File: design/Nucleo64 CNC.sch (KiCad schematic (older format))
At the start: 98 parts, among them J1 YMotor, J10 ZB, J11 AA, J12 AB, J13 VMOT, J14 Spindle/Coolant, J15 Control, J16 I2C, J17 UART/GPIO, J18 Limits, J19 GPIO, J2 XMotor, J20 Power out, J21 SDCARD/GPIO, J23 Reset, J24 DC Spindle, J3 ZMotor, J4 AMotor, J5 YA, J6 YB, J7 XA, J8 XB, J9 ZA, Q1 2N7002, Q2 IRLML6402, Q3 2N7002, U1 NUCLEO64-F411RE, U10 74LVC2G17, U2 TLP290-4, U3 TLP290-4, U4 TLP290-4, U5 24LC16, U6 TCA9406, U7 ULN2003, U8 TLP290-4, U9 74LVC1G17

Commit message: Updated
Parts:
- added C8: 2u2, Capacitor_SMD:C_1206_3216Metric, symbol Device:C
- added C9: 1u, Capacitor_SMD:C_1206_3216Metric, symbol Device:C
- added R37: 1M, Resistor_SMD:R_0805_2012Metric, symbol Device:R
- added U11: 74LVC1G17, Package_TO_SOT_SMD:SOT-353_SC-70-5, symbol IoEngineering:74LVC1G17
- added U12: TPS709, Package_TO_SOT_SMD:SOT-23-5, symbol Regulator_Linear:TC1017-xCT
- Lk6: value DC Spindle -> LDObypass
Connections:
- net +3V3: now also U9.5 (VCC)
- net +5V: now also U11.5 (VCC); no longer R1.1, R2.1, R24.1, R4.1, R5.1, R6.1, R7.1, R8.1, R9.1
- net AuxIn0: now also U1.66 (PB14); no longer U1.64 (PB15)
- net AuxIn1: now also U1.17 (PA15); no longer U1.60 (PB2)
- net AuxOut0: now also U1.64 (PB15); no longer U1.66 (PB14)
- net AuxOut1: now also U1.60 (PB2); no longer U1.63 (PB10)
- net Flood: now also U1.63 (PB10); no longer U1.65 (PB4)
- net GND: now also U9.3 (GND), R37.2, U11.3 (GND); no longer J15.1 (Pin_1), J15.3 (Pin_3), J15.5 (Pin_5), J15.7 (Pin_7), J15.9 (Pin_9), J18.1 (Pin_1), J18.3 (Pin_3), J18.5 (Pin_5), J18.7 (Pin_7), U2.11, U2.13, U2.15, U2.9, U3.11, U3.13, U3.15, U3.9, U8.9
- net Mist: now also U1.65 (PB4); no longer U1.68 (PB13)
- net STDiag1: now also U1.68 (PB13); no longer U1.17 (PA15)
- net SpindlePWM: now also U11.2; no longer J14.16 (Pin_16), Lk6.1 (Pin_1)
- net at U4.10, U4.12, U4.14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: now also Lk6.2 (Pin_2), C8.1, U12.5 (VOUT); no longer Lk1.2 (Pin_2), U7.9 (COM)
- net GNDS: now reaches J14.1 (Pin_1), J14.11 (Pin_11), J14.13 (Pin_13), J14.3 (Pin_3), J14.5 (Pin_5), J14.7 (Pin_7), J14.9 (Pin_9), Lk3.2 (Pin_2), U7.7 (I7), U7.8 (GND)
- net GNDS: now also J15.1 (Pin_1), J15.3 (Pin_3), J15.5 (Pin_5), J15.7 (Pin_7), J15.9 (Pin_9), J18.1 (Pin_1), J18.3 (Pin_3), J18.5 (Pin_5), J18.7 (Pin_7), U2.11, U2.13, U2.15, U2.9, U3.11, U3.13, U3.15, U3.9, U8.9, C8.2, C9.2, R37.1, U12.2 (GND)
- net SpindlePWMOut: now reaches U8.6
- net SpindlePWMOut: now also J14.16 (Pin_16), U11.4; no longer Lk6.2 (Pin_2)
- new net Vdrive: C9.1, Lk1.2 (Pin_2), Lk6.1 (Pin_1), R1.1, R2.1, R24.1, R4.1, R5.1, R6.1, R7.1, R8.1, R9.1, U12.1 (VIN)
- no-connect marks 10 -> 11
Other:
- moved on the sheet: Lk1, Lk7, U9

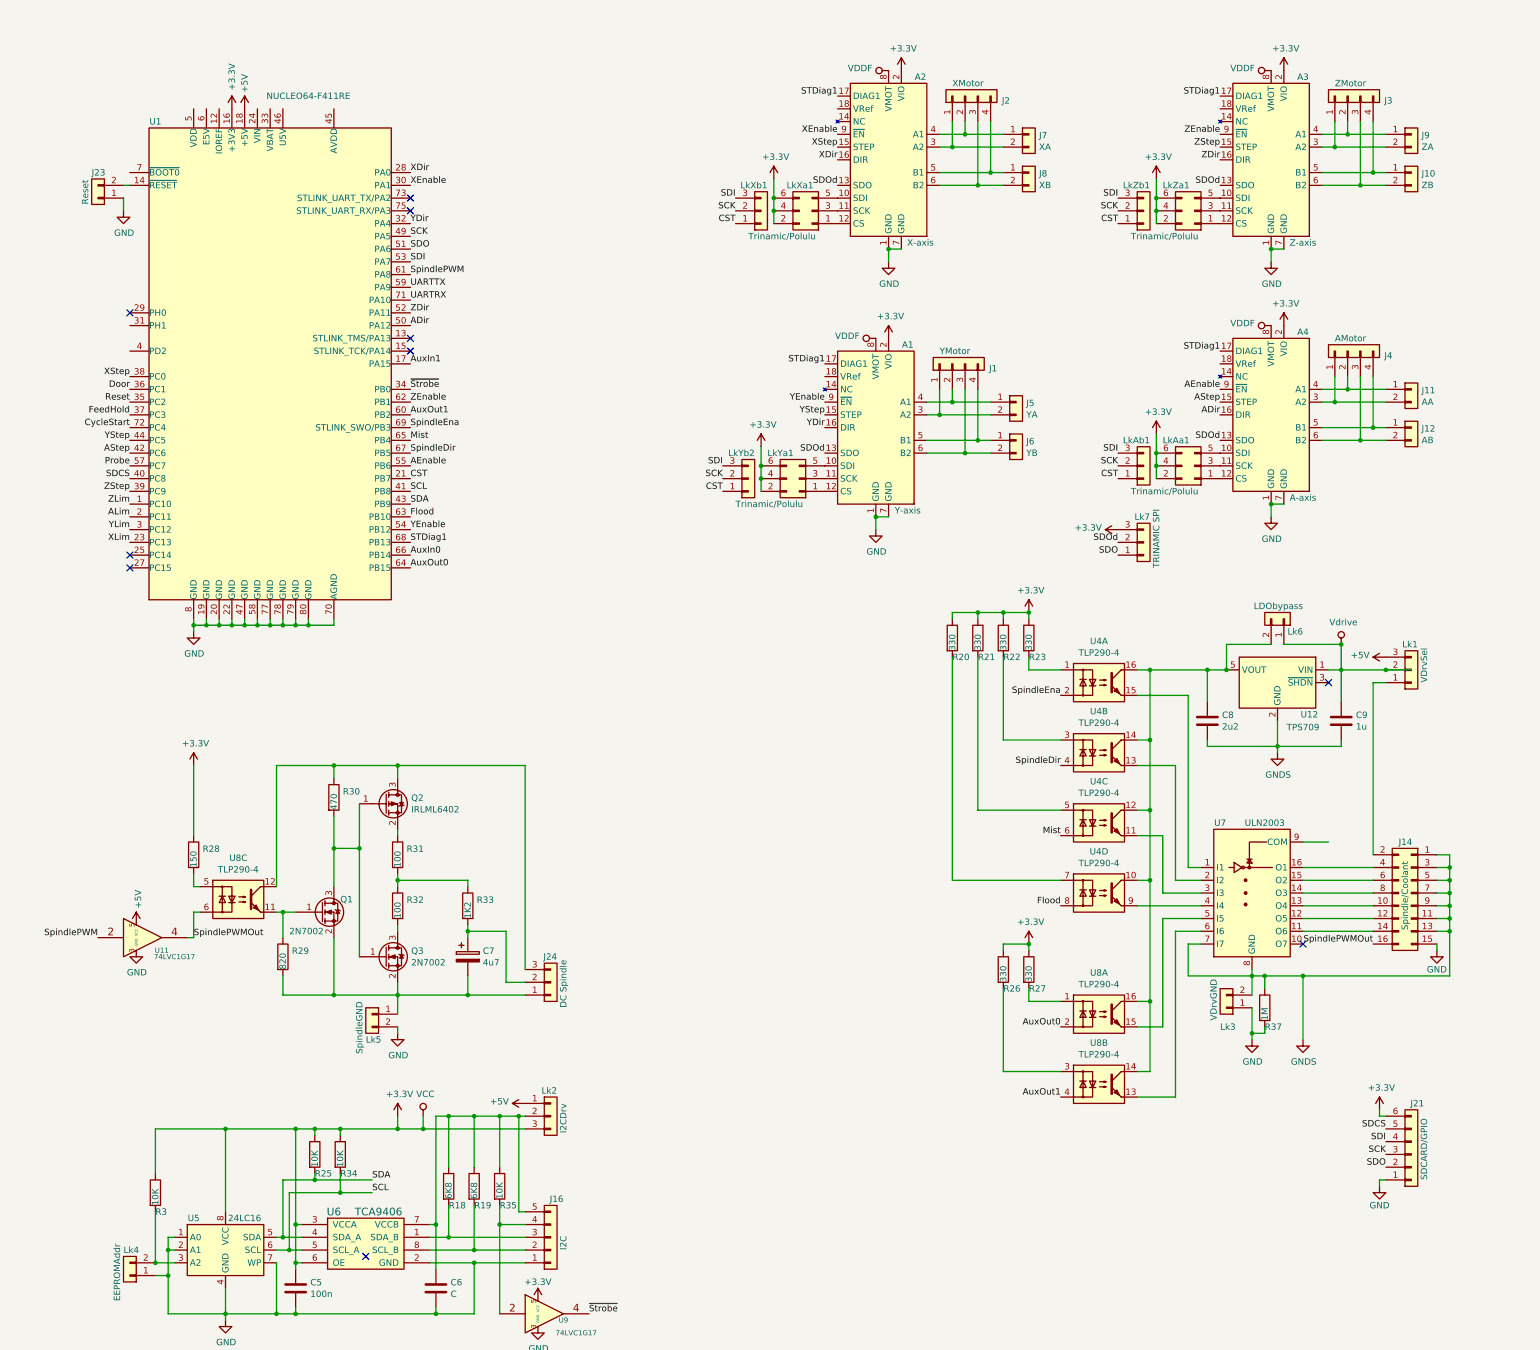
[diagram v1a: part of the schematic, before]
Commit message: Updated to version sent for small prototype batch
Design and board map file to be verified with this batch.
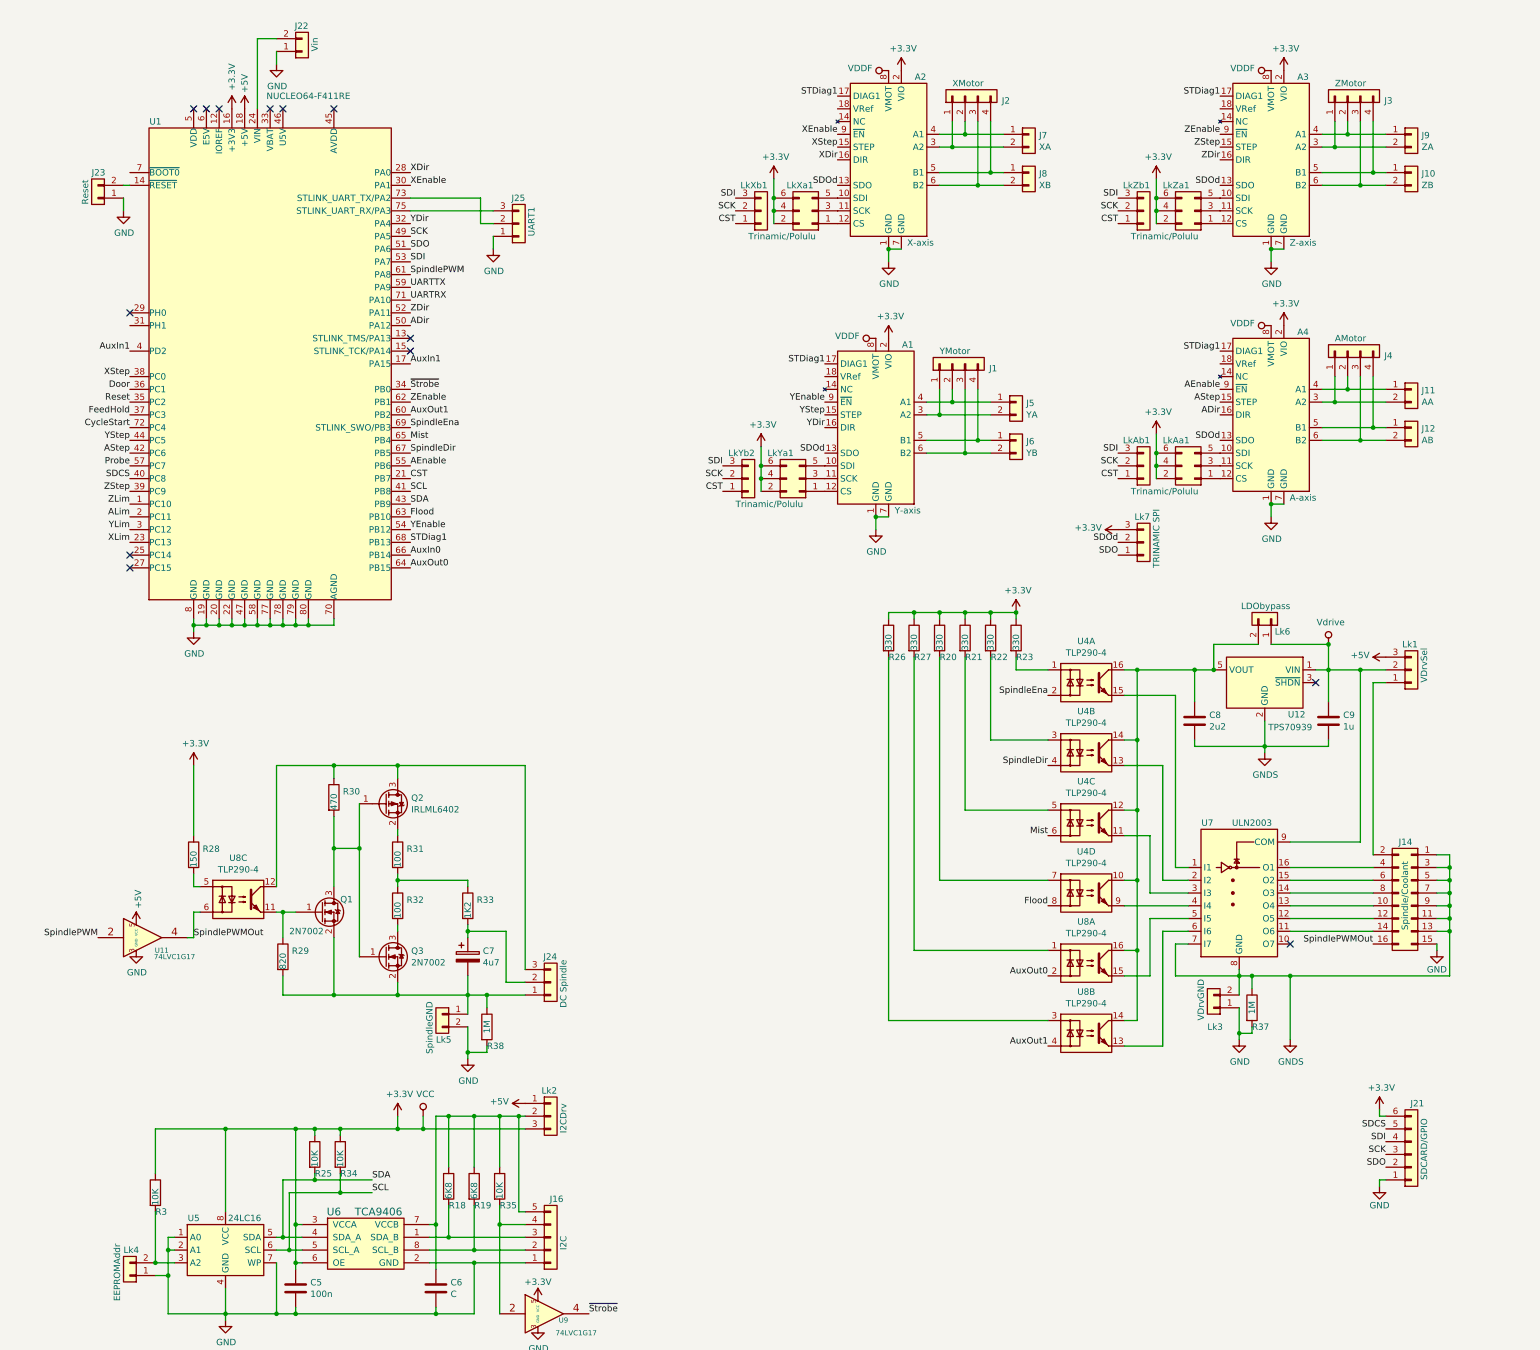
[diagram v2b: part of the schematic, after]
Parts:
- added J22: Vin, Connector_PinHeader_2.54mm:PinHeader_1x02_P2.54mm_Vertical, symbol Connector_Generic:Conn_01x02
- added J25: UART1, Connector_PinHeader_2.54mm:PinHeader_1x03_P2.54mm_Vertical, symbol Connector_Generic:Conn_01x03
- added R38: 1M, Resistor_SMD:R_0805_2012Metric, symbol Device:R
- U12: value TPS709 -> TPS70939
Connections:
- net AuxIn1: now also U1.4 (PD2)
- net GND: now also J22.1 (Pin_1), J25.1 (Pin_1), R38.2
- net Vdrive: now also U7.9 (COM)
- net at U1.24 (VIN): now also J22.2 (Pin_2)
- net at U1.73 (STLINK_UART_TX/PA2): now also J25.2 (Pin_2)
- net at U1.75 (STLINK_UART_RX/PA3): now also J25.3 (Pin_3)
- net at C7.2, J24.1 (Pin_1), Lk5.1 (Pin_1)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: now also R38.1
- no-connect marks 11 -> 14
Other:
- moved on the sheet: C8, C9, Lk3, Lk5, Lk6, R20, R21, R22, R23, R26, R27, R37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

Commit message: Updated to v1.0c
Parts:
- added Lk10, Lk11, Lk12, Lk9: AA, Connector_PinHeader_2.54mm:PinHeader_1x02_P2.54mm_Vertical, symbol Connector_Generic:Conn_01x02
- added Lk13: TMC UART, Connector_PinHeader_2.54mm:PinHeader_1x02_P2.54mm_Vertical, symbol Connector_Generic:Conn_01x02
- added Lk8: TMC UART/SPI, Connector_PinHeader_2.54mm:PinHeader_1x03_P2.54mm_Vertical, symbol Connector_Generic:Conn_01x03
- added R39: 1K, Resistor_SMD:R_0805_2012Metric, symbol Device:R
- added R40: 470, Resistor_SMD:R_0805_2012Metric, symbol Device:R
- added R41: 2K2, Resistor_SMD:R_0805_2012Metric, symbol Device:R
- added R42, R43: 10K, Resistor_SMD:R_0805_2012Metric, symbol Device:R
- added U13: VOM452, Package_SO:MFSOP6-5_4.4x3.6mm_P1.27mm, symbol IoEngineering:VOM452
- C7: value 4u7 -> 10u
- J17: value UART/GPIO -> UART
- J19: footprint Connector_PinHeader_2.54mm:PinHeader_1x03_P2.54mm_Vertical -> Connector_PinHeader_2.54mm:PinHeader_1x04_P2.54mm_Vertical; symbol Connector_Generic:Conn_01x03 -> Connector_Generic:Conn_01x04
- Lk7: value TRINAMIC SPI -> TMC DATA
- R28: value 150 -> 470
- R30: value 470 -> 1K2
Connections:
- net +3V3: now also LkAa1.1 (Pin_1), LkAa1.3 (Pin_3), LkAa1.5 (Pin_5), LkXa1.1 (Pin_1), LkXa1.3 (Pin_3), LkXa1.5 (Pin_5), LkYa1.1 (Pin_1), LkYa1.3 (Pin_3), LkYa1.5 (Pin_5), LkZa1.1 (Pin_1), LkZa1.3 (Pin_3), LkZa1.5 (Pin_5), R41.1; no longer LkAa1.2 (Pin_2), LkAa1.4 (Pin_4), LkAa1.6 (Pin_6), LkXa1.2 (Pin_2), LkXa1.4 (Pin_4), LkXa1.6 (Pin_6), LkYa1.2 (Pin_2), LkYa1.4 (Pin_4), LkYa1.6 (Pin_6), LkZa1.2 (Pin_2), LkZa1.4 (Pin_4), LkZa1.6 (Pin_6), R28.1
- net +5V: now also R28.1
- net ALim: now also A4.17 (DIAG1)
- net GND: now also R42.2, R43.2
- net GNDS: now also U8.11
- net Probe: now also U8.12; no longer U8.10
- net SDI: no longer LkAb1.3 (Pin_3), LkYb2.3 (Pin_3), LkZb1.3 (Pin_3)
- net SDO: now also Lk8.3 (Pin_3); no longer Lk7.1 (Pin_1)
- net SDOd: now also A1.14 (NC), A2.14 (NC), A3.14 (NC), A4.14 (NC), Lk10.1 (Pin_1), Lk11.1 (Pin_1), Lk12.1 (Pin_1), Lk9.1 (Pin_1); no longer A1.13 (SDO), A2.13 (SDO), A3.13 (SDO), A4.13 (SDO), Lk7.2 (Pin_2)
- net SpindlePWMOut: now also U13.3 (C); no longer U8.6
- net UARTRX: now also Lk13.1 (Pin_1)
- net UARTTX: now also R39.2
- net Vdrive: now also R40.1
- net XLim: now also A2.17 (DIAG1)
- net YLim: now also A1.17 (DIAG1)
- net ZLim: now also A3.17 (DIAG1)
- net at A2.10 (SDI): now also LkXa1.6 (Pin_6); no longer LkXa1.5 (Pin_5)
- net at A2.11 (SCK): now also LkXa1.4 (Pin_4); no longer LkXa1.3 (Pin_3)
- net at A2.12 (CS): now also LkXa1.2 (Pin_2); no longer LkXa1.1 (Pin_1)
- net at A1.10 (SDI): now also LkYa1.6 (Pin_6); no longer LkYa1.5 (Pin_5)
- net at A1.11 (SCK): now also LkYa1.4 (Pin_4); no longer LkYa1.3 (Pin_3)
- net at A1.12 (CS): now also LkYa1.2 (Pin_2); no longer LkYa1.1 (Pin_1)
- net at A3.10 (SDI): now also LkZa1.6 (Pin_6); no longer LkZa1.5 (Pin_5)
- net at A3.11 (SCK): now also LkZa1.4 (Pin_4); no longer LkZa1.3 (Pin_3)
- net at A3.12 (CS): now also LkZa1.2 (Pin_2); no longer LkZa1.1 (Pin_1)
- net at A4.10 (SDI): now also LkAa1.6 (Pin_6); no longer LkAa1.5 (Pin_5)
- net at A4.11 (SCK): now also LkAa1.4 (Pin_4); no longer LkAa1.3 (Pin_3)
- net at A4.12 (CS): now also LkAa1.2 (Pin_2); no longer LkAa1.1 (Pin_1)
- net at J19.2 (Pin_2), U10.3: now also R43.1
- net at J19.3 (Pin_3), U10.1: now also R42.1
- net at C7.2, J24.1 (Pin_1), Lk5.1 (Pin_1)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: now also U13.4 (GND); no longer R29.2
- net at Q2.2 (S): now also J24.3 (Pin_3), R29.1, R30.1, U13.6 (VCC); no longer R31.1
- net at U8.8: now also J19.4 (Pin_4); no longer J15.2 (Pin_2)
- net at R28.2: now also U13.1 (A); no longer U8.5
- net at R24.2: now also U8.5; no longer U8.7
- removed net STDiag1: A1.17 (DIAG1), A2.17 (DIAG1), A3.17 (DIAG1), A4.17 (DIAG1), U1.68 (PB13)
- new net: Lk7.1 (Pin_1), Lk8.2 (Pin_2)
- new net: Q1.1 (G), R29.2, U13.5 (VO)
- new net: Q2.3 (D), R31.1
- new net: J15.2 (Pin_2), U8.6
- new net: Lk13.2 (Pin_2), Lk8.1 (Pin_1), R39.1
- new net: R40.2, U8.7
- new net AuxIn2: R41.2, U1.68 (PB13), U8.10
- new net SDIa: A3.13 (SDO), Lk11.2 (Pin_2), LkAb1.3 (Pin_3)
- new net SDIy: A2.13 (SDO), Lk9.2 (Pin_2), LkYb2.3 (Pin_3)
- new net SDIz: A1.13 (SDO), Lk10.2 (Pin_2), LkZb1.3 (Pin_3)
- new net SDOt: A4.13 (SDO), Lk12.2 (Pin_2), Lk7.2 (Pin_2)
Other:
- moved on the sheet: J17, Lk7, Q1, R10, R12, R14, R16, R29, R36, U11, U3A, U3B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
